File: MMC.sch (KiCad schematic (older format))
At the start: 53 parts, among them SW2 SW_Push, SW3 KSS241GLFS, U2 LPC1776FET180,551, Y5 XTAL_8MHZ_TXC_7A-8.000MAAE-T

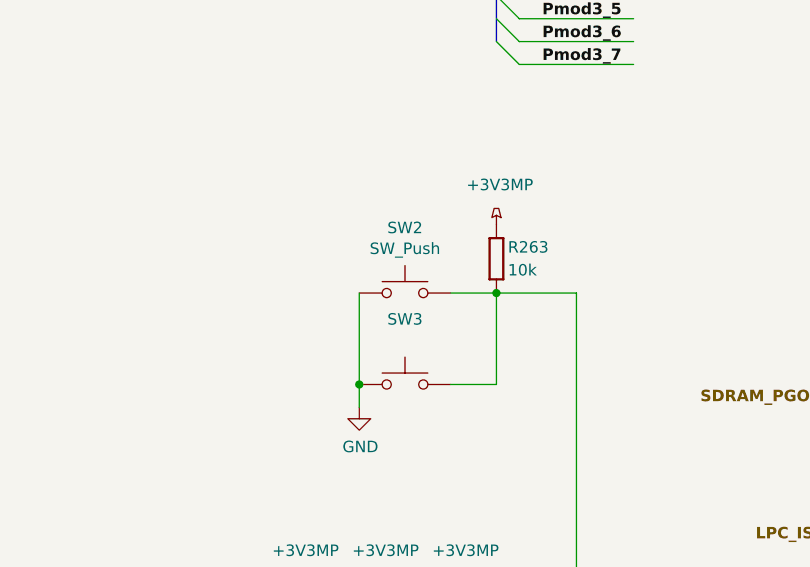
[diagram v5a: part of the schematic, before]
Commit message: BOM configuration file edited, updated Marble picture, some components part number changed
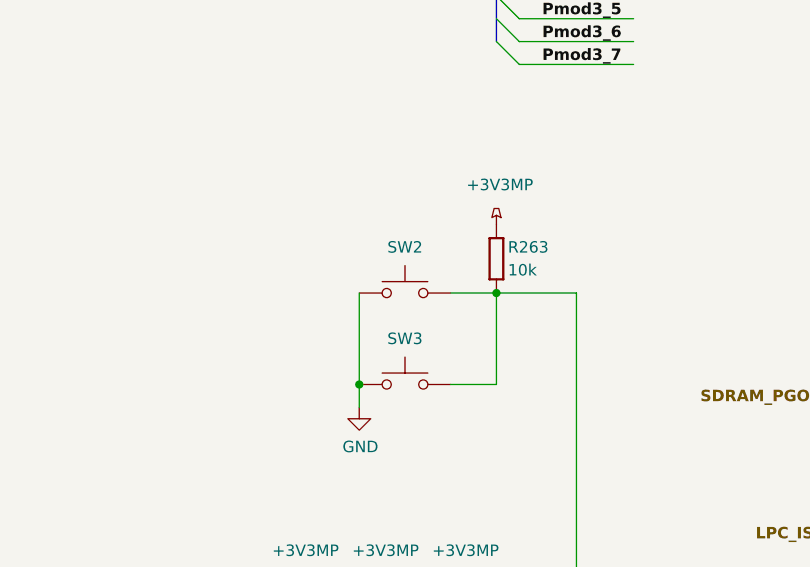
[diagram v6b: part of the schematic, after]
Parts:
- D3: Manufacturer Part Number BAT165 -> BAT165AX
- SW2: value SW_Push -> SKHHLQA010; Manufacturer Part Number (none) -> SKHHLQA010
- SW3: Manufacturer Part Number (none) -> KSS241GLFS
- U2: Manufacturer Part Number (none) -> LPC1776FET180,551; PN LPC1776FET180,551 -> (none)
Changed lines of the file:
@@
 $Descr A3 16535 11693
 encoding utf-8
-Sheet 24 25
+Sheet 23 25
 Title "Marble"
 Date "2019-01-16"
@@
 F 2 "ICs And Semiconductors SMD_BGA:BGA180C80P14X14_1200X1200X120" H 9300 9100 50  0001 C CNN
 F 3 "" H 9300 9100 50  0001 C CNN
-F 4 "LPC1776FET180,551" H 8600 7800 50  0001 C CNN "PN"
+F 4 "LPC1776FET180,551" H 8600 7800 50  0001 C CNN "Manufacturer Part Number"
 	5    8600 7800
 	1    0    0    -1
@@
 F 2 "ICs And Semiconductors SMD_BGA:BGA180C80P14X14_1200X1200X120" H 5250 2150 50  0001 C CNN
 F 3 "" H 5250 2150 50  0001 C CNN
-F 4 "LPC1776FET180,551" H 4550 850 50  0001 C CNN "PN"
+F 4 "LPC1776FET180,551" H 4550 850 50  0001 C CNN "Manufacturer Part Number"
 	1    4550 850
 	1    0    0    -1
@@
 F 2 "ICs And Semiconductors SMD_BGA:BGA180C80P14X14_1200X1200X120" H 13750 6000 50  0001 C CNN
 F 3 "" H 13750 6000 50  0001 C CNN
-F 4 "LPC1776FET180,551" H 13050 4700 50  0001 C CNN "PN"
+F 4 "LPC1776FET180,551" H 13050 4700 50  0001 C CNN "Manufacturer Part Number"
 	2    13050 4700
 	1    0    0    -1
@@
 F 2 "ICs And Semiconductors SMD_BGA:BGA180C80P14X14_1200X1200X120" H 3450 9600 50  0001 C CNN
 F 3 "" H 3450 9600 50  0001 C CNN
-F 4 "LPC1776FET180,551" H 2750 8300 50  0001 C CNN "PN"
+F 4 "LPC1776FET180,551" H 2750 8300 50  0001 C CNN "Manufacturer Part Number"
 	4    2750 8300
 	1    0    0    -1
@@
 F 15 "Medium Power AF Schottky Diode" H 2250 7010 60  0001 L CNN "Part Description"
 F 16 "INFINEON" H 2250 6920 60  0001 L CNN "Manufacturer"
-F 17 "BAT165" H 2250 6830 60  0001 L CNN "Manufacturer Part Number"
+F 17 "BAT165AX" H 2250 6830 60  0001 L CNN "Manufacturer Part Number"
 F 18 "2" H 2250 6740 60  0001 L CNN "Pin Count"
 F 19 "SOD323" H 2250 6650 60  0001 L CNN "Case"
@@
 U 1 1 5DC8E1FA
 P 10050 4750
-F 0 "SW2" H 10050 5035 50  0000 C CNN
-F 1 "SW_Push" H 10050 4944 50  0000 C CNN
+F 0 "SW2" H 10050 4950 50  0000 C CNN
+F 1 "SKHHLQA010" H 10050 4944 50  0001 C CNN
 F 2 "Switches:PB_ALPS_SKHHLQA010" H 10050 4950 50  0001 C CNN
 F 3 "PB_ALPS_SKHHLQA010" H 10050 4950 50  0001 C CNN
+F 4 "SKHHLQA010" H 10050 4750 50  0001 C CNN "Manufacturer Part Number"
 	1    10050 4750
 	1    0    0    -1
@@
 F 2 "ICs And Semiconductors SMD_BGA:BGA180C80P14X14_1200X1200X120" H 13750 1950 50  0001 C CNN
 F 3 "" H 13750 1950 50  0001 C CNN
-F 4 "LPC1776FET180,551" H 13050 650 50  0001 C CNN "PN"
+F 4 "LPC1776FET180,551" H 13050 650 50  0001 C CNN "Manufacturer Part Number"
 	3    13050 650
 	1    0    0    -1
@@
 AR Path="/5CF2A4CC" Ref="SW?"  Part="1"
 AR Path="/5BCEDA39/5CF2A4CC" Ref="SW3"  Part="1"
-F 0 "SW3" H 10050 5435 50  0000 C CNN
+F 0 "SW3" H 10050 5350 50  0000 C CNN
 F 1 "KSS241GLFS" H 10050 5344 50  0001 C CNN
 F 2 "AG5300_2:KSS241GLFS" H 10050 5350 50  0001 C CNN
 F 3 "KSS241GLFS" H 10050 5350 50  0001 C CNN
+F 4 "KSS241GLFS" H 10050 5150 50  0001 C CNN "Manufacturer Part Number"
 	1    10050 5150
 	1    0    0    -1

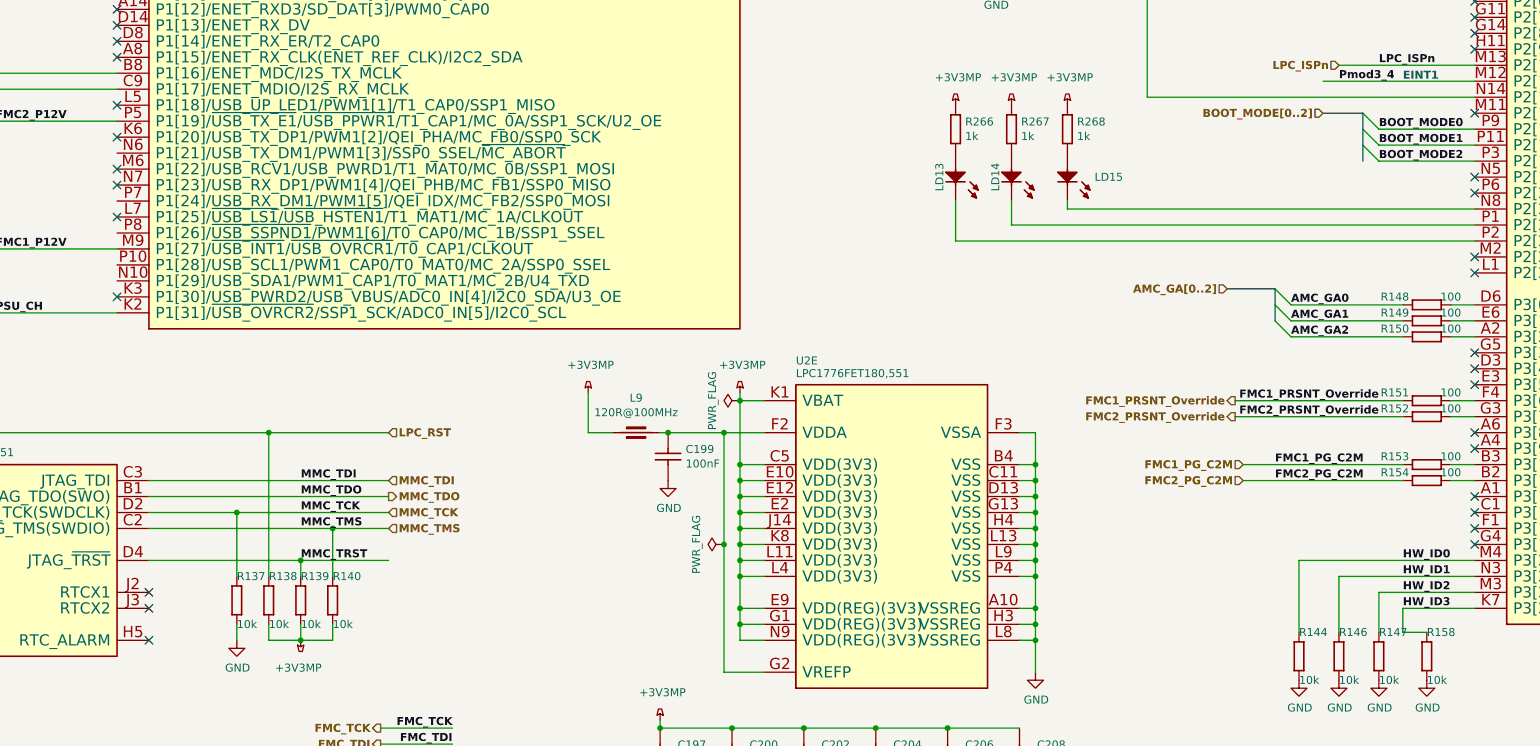
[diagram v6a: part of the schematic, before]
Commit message: README edited, less ERC errors and warnings
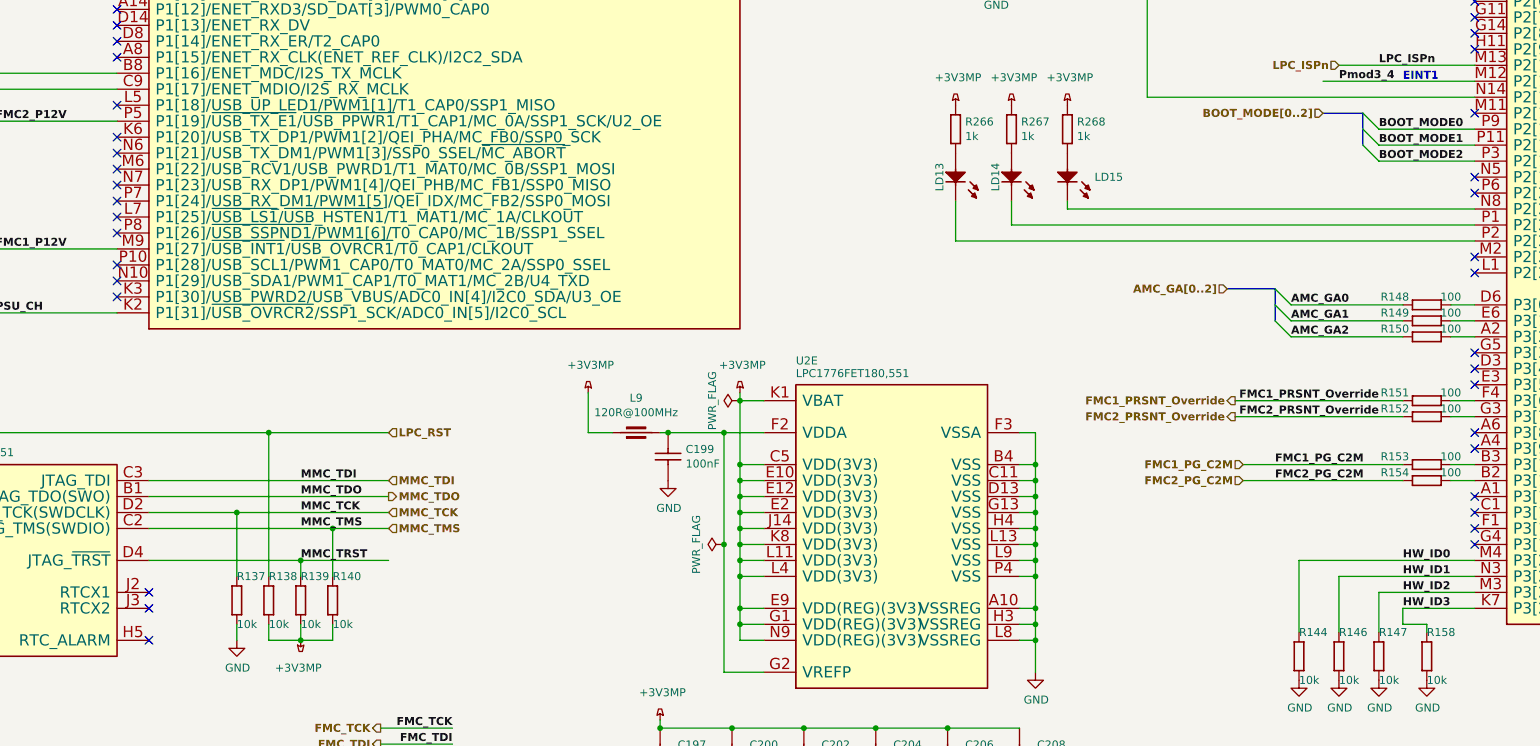
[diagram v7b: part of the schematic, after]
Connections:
- wire segments 236 -> 237
- no-connect marks 81 -> 86
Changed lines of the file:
@@
 	12250 9100 12850 9100
 Wire Wire Line
-	12550 9350 12400 9350
-Wire Wire Line
-	12400 9350 12400 9200
-Wire Wire Line
 	12000 9350 12000 9000
 Wire Wire Line
@@
 Wire Wire Line
 	11350 8000 12400 8000
+Wire Wire Line
+	12400 9200 12400 9300
+Wire Wire Line
+	12400 9300 12550 9300
+Wire Wire Line
+	12550 9300 12550 9350
+NoConn ~ 4350 6350
+NoConn ~ 4350 6650
+NoConn ~ 4350 6850
+NoConn ~ 4350 7050
+NoConn ~ 4350 7150
 Wire Bus Line
 	11600 7200 11600 7400
 Wire Bus Line
-	12150 6100 12150 6400
+	12150 6100 12150 6300
 Wire Bus Line
 	10450 2900 10450 3650
